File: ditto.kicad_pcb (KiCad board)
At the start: 2 copper layers, 257 x 91 mm, 136 parts, among them J1 Conn_01x21, J2 USB_C_Receptacle_USB2.0, SW1 SW_Push, SW10 SW_Push, SW11 SW_Push, SW12 SW_Push, SW13 SW_Push, SW14 SW_Push, SW15 SW_Push, SW16 SW_Push, SW17 SW_Push, SW18 SW_Push, SW19 SW_Push, SW2 SW_Push, SW20 SW_Push, SW21 SW_Push, SW22 SW_Push, SW23 SW_Push, SW24 SW_Push, SW25 SW_Push, SW26 SW_Push, SW27 SW_Push, SW28 SW_Push, SW29 SW_Push, SW3 SW_Push, SW30 SW_Push, SW31 SW_Push, SW32 SW_Push, SW33 SW_Push, SW34 SW_Push, SW35 SW_Push, SW36 SW_Push, SW37 SW_Push, SW38 SW_Push, SW39 SW_Push, SW4 SW_Push, SW40 SW_Push, SW5 SW_Push, SW6 SW_Push, SW7 SW_Push, SW8 SW_Push, SW9 SW_Push, U1 RP2040, U2 AP2112K-3.3, U3 W25Q128JVS, Y1 Crystal_GND24

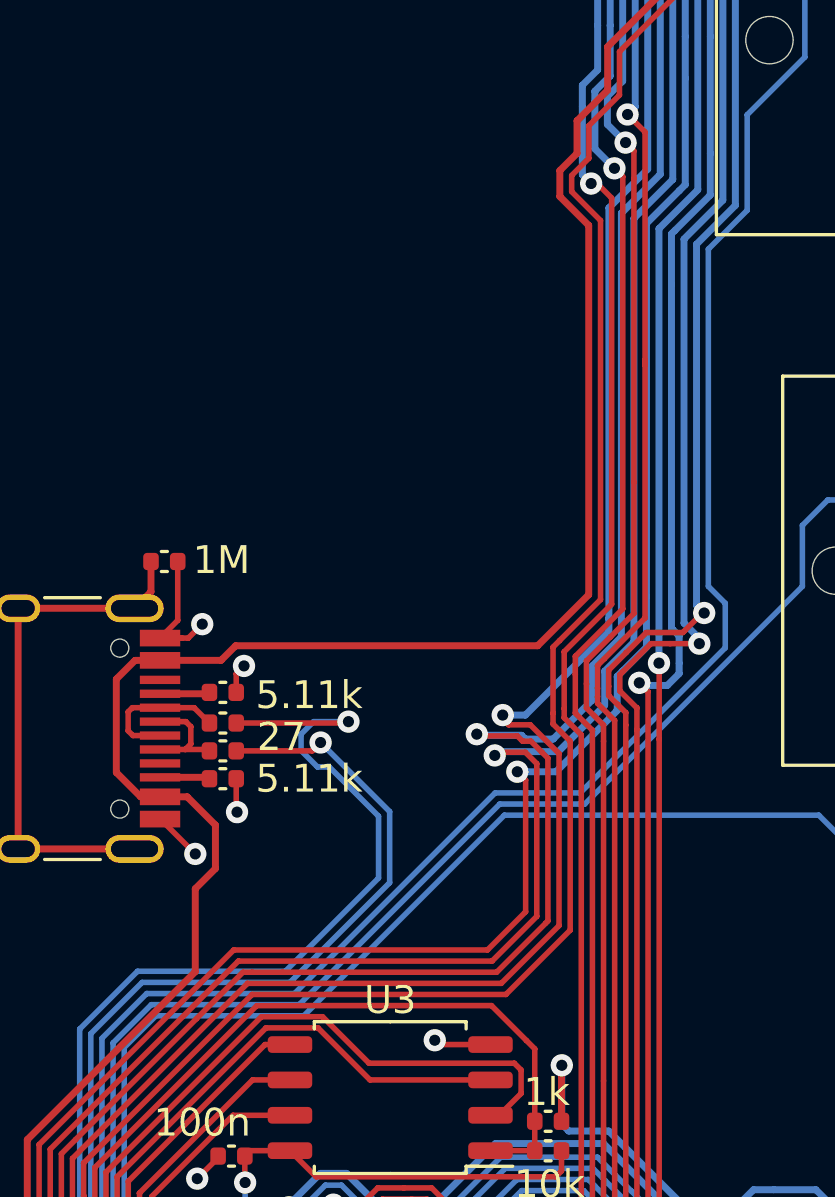
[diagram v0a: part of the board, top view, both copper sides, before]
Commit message: added logic level shifter for neopixels, gerbers, 3d file
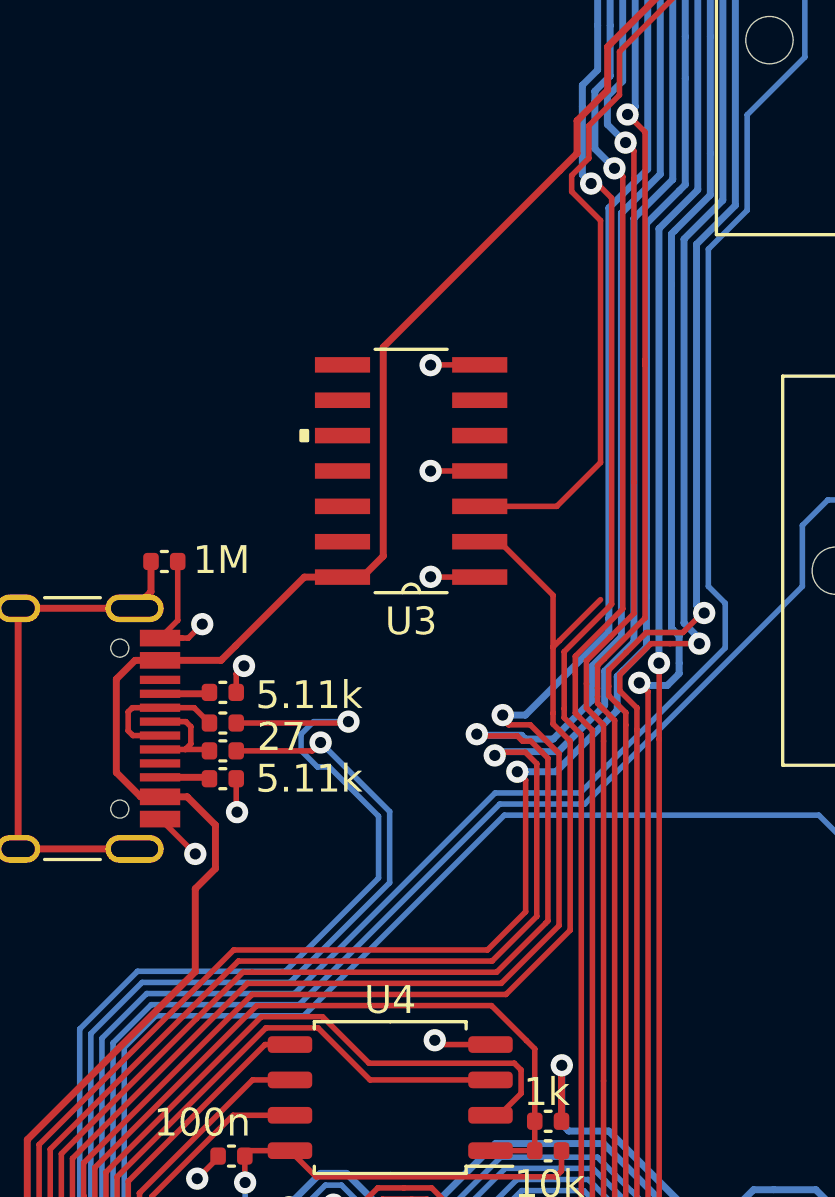
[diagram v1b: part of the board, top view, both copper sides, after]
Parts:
- added U3: SN74AHCT125QDRG4Q1, dip:SN74AHCT125QDRG4Q1, F.Cu at (118.5, 155.5)
- renumbered U3 to U4
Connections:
- R1 pad 2: /LEDS -> /LEDS_5V
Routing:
- net /LEDS_5V: track 0.00 -> 44.5 mm
- net /LEDS: track 107.1 -> 67.9 mm
- net +5V: track 475.7 -> 469.7 mm
- net GND: track 114.0 -> 119.3 mm, vias 20 -> 23
